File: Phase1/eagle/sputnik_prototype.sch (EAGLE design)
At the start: 61 parts, among them U1 MEGA128-M, Y1 32MHz, Y2 8MHZ

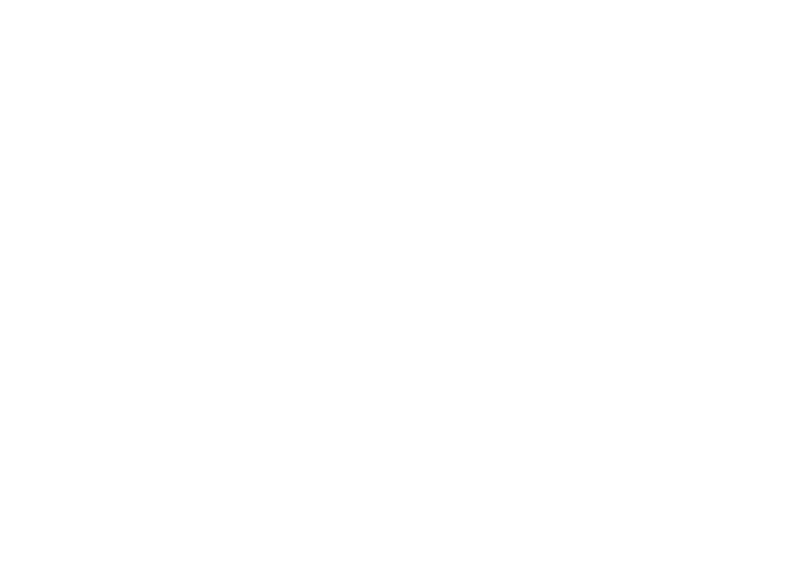
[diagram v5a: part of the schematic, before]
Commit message: Created LDO and fixed PA footprints
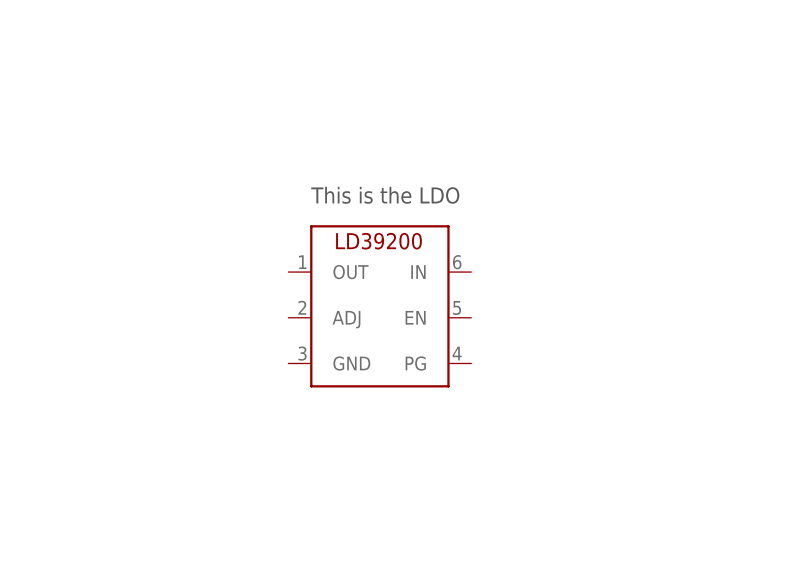
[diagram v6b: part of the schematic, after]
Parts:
- added U$6: SKY65116, psas_c3_team05:SKY65116
- U$3: value SKY65116 -> LD39200; device psas_c3_team05:SKY65116 -> psas_c3_team05:LD39200
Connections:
- net GND: now also U$6.GND, U$6.GND1, U$6.GND2, U$6.GND3, U$6.GND4, U$6.GND5; no longer U$3.GND, U$3.GND1, U$3.GND2, U$3.GND3, U$3.GND4, U$3.GND5
- net N$21: now also U$6.RFIN; no longer U$3.RFIN
- net N$22: now also U$6.RFOUT; no longer U$3.RFOUT
- net V+: now also U$6.VCC1, U$6.VCC2, U$6.VCNT, U$6.VREF; no longer U$3.VCC1, U$3.VCC2, U$3.VCNT, U$3.VREF
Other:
- note added: "This is the LDO"
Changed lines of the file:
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@@
 <?xml version="1.0" encoding="utf-8"?>
 <!DOCTYPE eagle SYSTEM "eagle.dtd">
-<eagle version="7.3.0">
+<eagle version="7.4.0">
 <drawing>
 <settings>
@@
 <part name="U$2" library="psas_c3_team05" deviceset="SMAJ716-ND" device=""/>
 <part name="GND13" library="psas_c3_team05" deviceset="GND" device=""/>
-<part name="U$3" library="psas_c3_team05" deviceset="SKY65116" device=""/>
 <part name="GND14" library="psas_c3_team05" deviceset="GND" device=""/>
 <part name="GND15" library="psas_c3_team05" deviceset="GND" device=""/>
@@
 <part name="Y2" library="Lilypad_Arduino_USB_v12" deviceset="SPARKFUN-FREQCTRL_RESONATOR" device="8MHZ" value="8MHZ"/>
 <part name="JP4" library="pinhead" deviceset="PINHD-1X5" device="5X2MM"/>
+<part name="U$6" library="psas_c3_team05" deviceset="SKY65116" device=""/>
+<part name="U$3" library="psas_c3_team05" deviceset="LD39200" device=""/>
 </parts>
 <sheets>
@@
 <text x="17.78" y="233.68" size="1.778" layer="97">power</text>
 <text x="15.24" y="195.58" size="1.778" layer="97">control</text>
+<text x="345.44" y="264.16" size="1.778" layer="97">This is the LDO</text>
 </plain>
 <instances>
@@
 <instance part="U$2" gate="G$1" x="543.56" y="307.34" rot="MR0"/>
 <instance part="GND13" gate="1" x="543.56" y="294.64"/>
-<instance part="U$3" gate="G$1" x="426.72" y="383.54"/>
 <instance part="GND14" gate="1" x="403.86" y="365.76"/>
 <instance part="GND15" gate="1" x="462.28" y="373.38"/>
@@
 </instance>
 <instance part="JP4" gate="A" x="27.94" y="195.58" rot="MR0"/>
+<instance part="U$6" gate="G$1" x="426.72" y="383.54"/>
+<instance part="U$3" gate="G$1" x="345.44" y="261.62"/>
 </instances>
 <busses>
@@
 <segment>
 <pinref part="GND14" gate="1" pin="GND"/>
-<pinref part="U$3" gate="G$1" pin="GND"/>
 <wire x1="403.86" y1="368.3" x2="403.86" y2="375.92" width="0.1524" layer="91"/>
 <wire x1="403.86" y1="375.92" x2="403.86" y2="378.46" width="0.1524" layer="91"/>
@@
 <wire x1="403.86" y1="383.54" x2="403.86" y2="388.62" width="0.1524" layer="91"/>
 <wire x1="403.86" y1="388.62" x2="414.02" y2="388.62" width="0.1524" layer="91"/>
-<pinref part="U$3" gate="G$1" pin="GND1"/>
 <wire x1="414.02" y1="383.54" x2="403.86" y2="383.54" width="0.1524" layer="91"/>
 <junction x="403.86" y="383.54"/>
-<pinref part="U$3" gate="G$1" pin="GND2"/>
 <wire x1="414.02" y1="378.46" x2="403.86" y2="378.46" width="0.1524" layer="91"/>
 <junction x="403.86" y="378.46"/>
-<pinref part="U$3" gate="G$1" pin="GND3"/>
 <wire x1="414.02" y1="375.92" x2="403.86" y2="375.92" width="0.1524" layer="91"/>
 <junction x="403.86" y="375.92"/>
-</segment>
-<segment>
-<pinref part="U$3" gate="G$1" pin="GND4"/>
+<pinref part="U$6" gate="G$1" pin="GND"/>
+<pinref part="U$6" gate="G$1" pin="GND2"/>
+<pinref part="U$6" gate="G$1" pin="GND3"/>
+<pinref part="U$6" gate="G$1" pin="GND1"/>
+</segment>
+<segment>
 <pinref part="GND15" gate="1" pin="GND"/>
 <wire x1="439.42" y1="388.62" x2="462.28" y2="388.62" width="0.1524" layer="91"/>
 <wire x1="462.28" y1="388.62" x2="462.28" y2="383.54" width="0.1524" layer="91"/>
-<pinref part="U$3" gate="G$1" pin="GND5"/>
 <wire x1="462.28" y1="383.54" x2="462.28" y2="375.92" width="0.1524" layer="91"/>
 <wire x1="439.42" y1="383.54" x2="462.28" y2="383.54" width="0.1524" layer="91"/>
 <junction x="462.28" y="383.54"/>
+<pinref part="U$6" gate="G$1" pin="GND4"/>
+<pinref part="U$6" gate="G$1" pin="GND5"/>
 </segment>
 <segment>
@@
 </segment>
 <segment>
-<pinref part="U$3" gate="G$1" pin="VCC1"/>
 <wire x1="414.02" y1="381" x2="408.94" y2="381" width="0.1524" layer="91"/>
 <wire x1="408.94" y1="381" x2="408.94" y2="414.02" width="0.1524" layer="91"/>
@@
 <junction x="416.56" y="414.02"/>
 <pinref part="SUPPLY5" gate="1" pin="V+"/>
+<pinref part="U$6" gate="G$1" pin="VCC1"/>
 </segment>
 <segment>
@@
 <wire x1="444.5" y1="414.02" x2="444.5" y2="381" width="0.1524" layer="91"/>
 <junction x="454.66" y="414.02"/>
-<pinref part="U$3" gate="G$1" pin="VCC2"/>
 <wire x1="444.5" y1="381" x2="439.42" y2="381" width="0.1524" layer="91"/>
+<pinref part="U$6" gate="G$1" pin="VCC2"/>
 </segment>
 <segment>
@@
 <junction x="487.68" y="347.98"/>
 <pinref part="C20" gate="CE" pin="2"/>
-<pinref part="U$3" gate="G$1" pin="VREF"/>
 <wire x1="439.42" y1="375.92" x2="457.2" y2="375.92" width="0.1524" layer="91"/>
 <wire x1="457.2" y1="375.92" x2="457.2" y2="347.98" width="0.1524" layer="91"/>
 <wire x1="457.2" y1="347.98" x2="477.52" y2="347.98" width="0.1524" layer="91"/>
 <junction x="477.52" y="347.98"/>
-</segment>
-<segment>
-<pinref part="U$3" gate="G$1" pin="VCNT"/>
+<pinref part="U$6" gate="G$1" pin="VREF"/>
+</segment>
+<segment>
 <wire x1="439.42" y1="378.46" x2="477.52" y2="378.46" width="0.1524" layer="91"/>
 <wire x1="477.52" y1="378.46" x2="487.68" y2="378.46" width="0.1524" layer="91"/>
@@
 <pinref part="C22" gate="CE" pin="2"/>
 <junction x="487.68" y="378.46"/>
+<pinref part="U$6" gate="G$1" pin="VCNT"/>
 </segment>
 <segment>
@@
 <pinref part="C14" gate="CE" pin="1"/>
 <wire x1="365.76" y1="386.08" x2="414.02" y2="386.08" width="0.1524" layer="91"/>
-<pinref part="U$3" gate="G$1" pin="RFIN"/>
+<pinref part="U$6" gate="G$1" pin="RFIN"/>
 </segment>
 </net>
 <net name="N$22" class="0">
 <segment>
-<pinref part="U$3" gate="G$1" pin="RFOUT"/>
 <wire x1="439.42" y1="386.08" x2="452.12" y2="386.08" width="0.1524" layer="91"/>
 <wire x1="452.12" y1="386.08" x2="452.12" y2="330.2" width="0.1524" layer="91"/>
@@
 <wire x1="452.12" y1="330.2" x2="500.38" y2="330.2" width="0.1524" layer="91"/>
 <wire x1="500.38" y1="330.2" x2="500.38" y2="322.58" width="0.1524" layer="91"/>
-</segment>
-</net>
+<pinref part="U$6" gate="G$1" pin="RFOUT"/>
+</segment>
+</net>

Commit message: Finished hooking up interfaces and power stuff
Created board file from schematic so its f/b annotated now. Hooked up LDO for KW0x and ATMEGA128. Other minor changes.
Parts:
- removed U$3: LD39200, psas_c3_team05:LD39200
- added C40: 2.2uF, rcl_custom:C-EU0603-B-NOSILK
- added C41: 100nF, rcl_custom:C-EU0603-B-NOSILK
- added C42: 470pF, rcl_custom:C-EU0603-B-NOSILK
- added JP5, JP6: (no value), psas_c3_team05:PINHD-1X2
- added JP7: (no value), pinhead:PINHD-1X3
- added TP1, TP10, TP11, TP12, TP13, TP14, TP15, TP2, TP3, TP4, TP5, TP7, TP8, TP9: TPSPAD1-13, testpad:TPSPAD1-13
- added U2: MIC5219 3.3V, Lilypad_Arduino_USB_v12:SPARKFUN-POWERIC_V_REG_MIC52193.3V
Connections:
- new net 3.3V: C26.1, C27.1, C28.2, C29.2, C30.2, C31.2, C36.2, C37.2, C38.2, C39.2, C40.2, J1.VDD, JP3.4, JP3.7, TP1.PP, U$1.VBAT1, U$1.VBAT2, U$1.VDD, U$1.VDD2, U$1.VDDA, U$1.VREFH, U1.AREF, U1.AVCC, U1.VCC, U1.VCC@1, U2.OUT
- new net N$1: U$1.PTA1, U1.(TXD/PDO)PE1
- new net N$2: U$1.PTA2, U1.(RXD/PDI)PE0
- new net N$3: C42.2, U2.BP
- new net PE4: JP7.1, TP7.PP, U1.(OC3B/INT4)PE4
- new net PE5: JP7.2, TP8.PP, U1.(OC3C/INT5)PE5
- new net PE6: JP7.3, TP9.PP, U1.(T3/INT6)PE6
- new net UART1_RX: JP5.1, TP4.PP, U$1.PTC3
- new net UART1_TX: JP5.2, TP5.PP, U$1.PTC4
- net DIO5/CLKOUT: now also TP15.PP
- net GND: now also C40.1, C41.1, C42.1, U2.GND
- net PA3: now also TP10.PP
- net PA4: now also TP11.PP
- net PA5: now also TP12.PP
- net PA6: now also TP13.PP
- net PA7: now also TP14.PP
- net PTA20/!RESET: now also U1.(OC3A/AIN1)PE3
- net SDA: now also JP6.2, TP3.PP
- net SDL: now also JP6.1, TP2.PP
- net V+: now also C41.2, U2.EN, U2.IN; no longer C26.1, C27.1, C28.2, C29.2, C30.2, C31.2, C36.2, C37.2, C38.2, C39.2, J1.VDD, JP3.4, JP3.7, U$1.VBAT1, U$1.VBAT2, U$1.VDD, U$1.VDD2, U$1.VDDA, U$1.VREFH, U1.AREF, U1.AVCC, U1.VCC, U1.VCC@1
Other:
- note added: "Payload interface"
- note added: "Sense"
- note added: "UART"
- note added: "UART connection between KW0x and ATMega128 PTA1 = KW0x UART0 RX PTA2 = KW0x UART0 TX PE1 = ATMega128 UART0 TX PE0 = ATMega128 UART0 RX PE1 is connected to PTA1 PE0 is connected to PTA2"
- note removed: "This is the LDO"

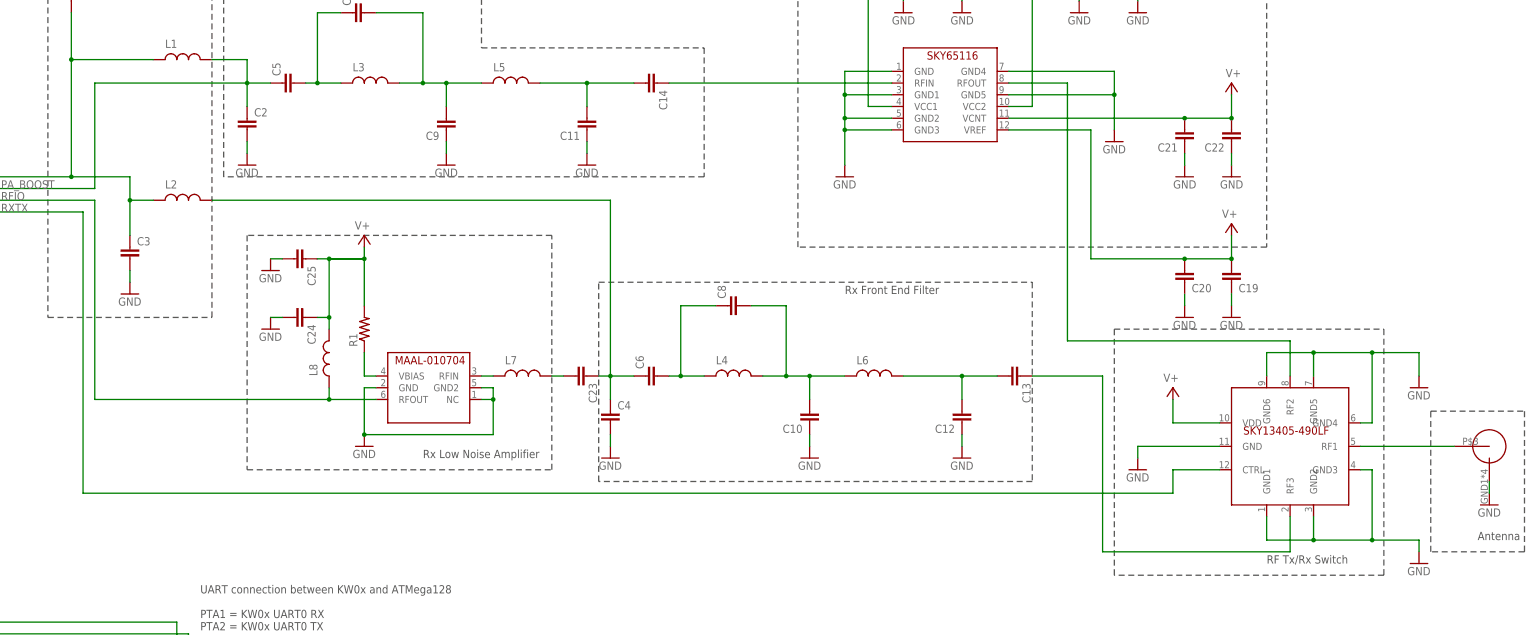
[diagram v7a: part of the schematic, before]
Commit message: Updated RF schematic
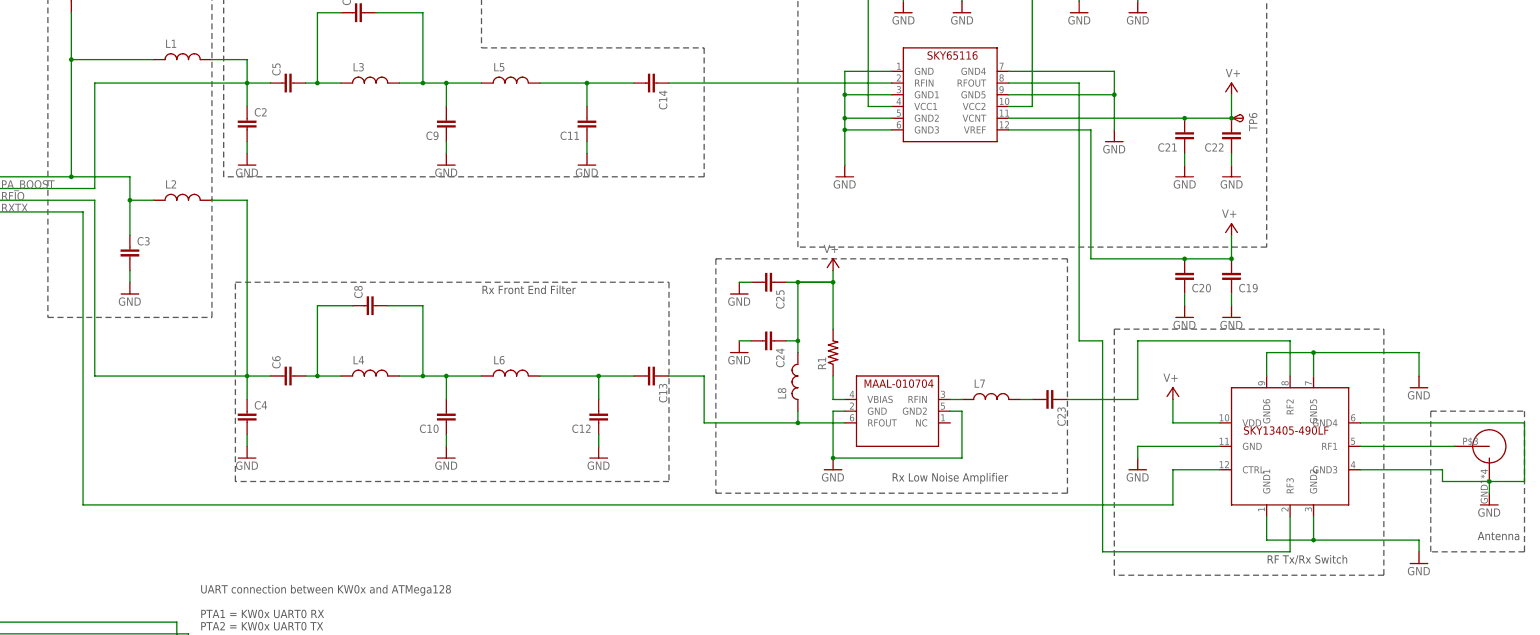
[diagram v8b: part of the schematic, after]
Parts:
- added TP6: TPSPAD1-13, testpad:TPSPAD1-13
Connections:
- removed net N$26: C13.1, U$5.RF3
- removed net N$33: C23.1, C4.1, C6.1, L2.2
- new net N$4: C13.1, L8.1, U$4.RFOUT
- new net N$5: C23.1, U$5.RF2
- net GND: no longer U$4.NC
- net N$22: now also U$5.RF3; no longer U$5.RF2
- net RFIO: now also C4.1, C6.1, L2.2; no longer L8.1, U$4.RFOUT
- net V+: now also TP6.PP
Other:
- moved on the sheet: C10, C12, C13, C23, C24, C25, C4, C6, C8, L4, L6, L7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
